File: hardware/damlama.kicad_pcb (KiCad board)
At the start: 2 copper layers, 91 x 90 mm, 63 parts, among them J1 173950578, J2 173950378, J3 SW, J4 PJ-002A, J5 RELAY, J6 SENSOR, J8 629105150521, K1 SRD-05VDC-SL-C, Q1 BC847, SW1 BTN_ACT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

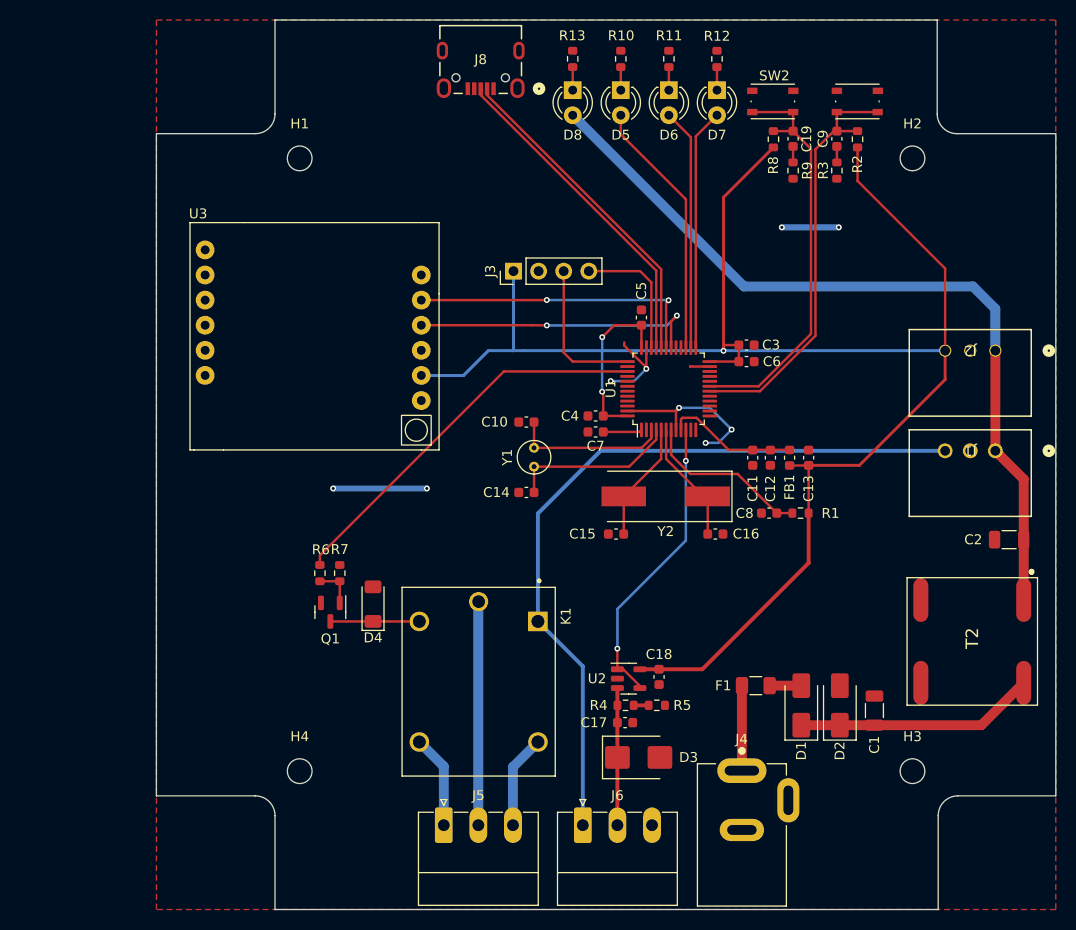
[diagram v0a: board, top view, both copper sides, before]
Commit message: MCU BOOT0 mistake fixed
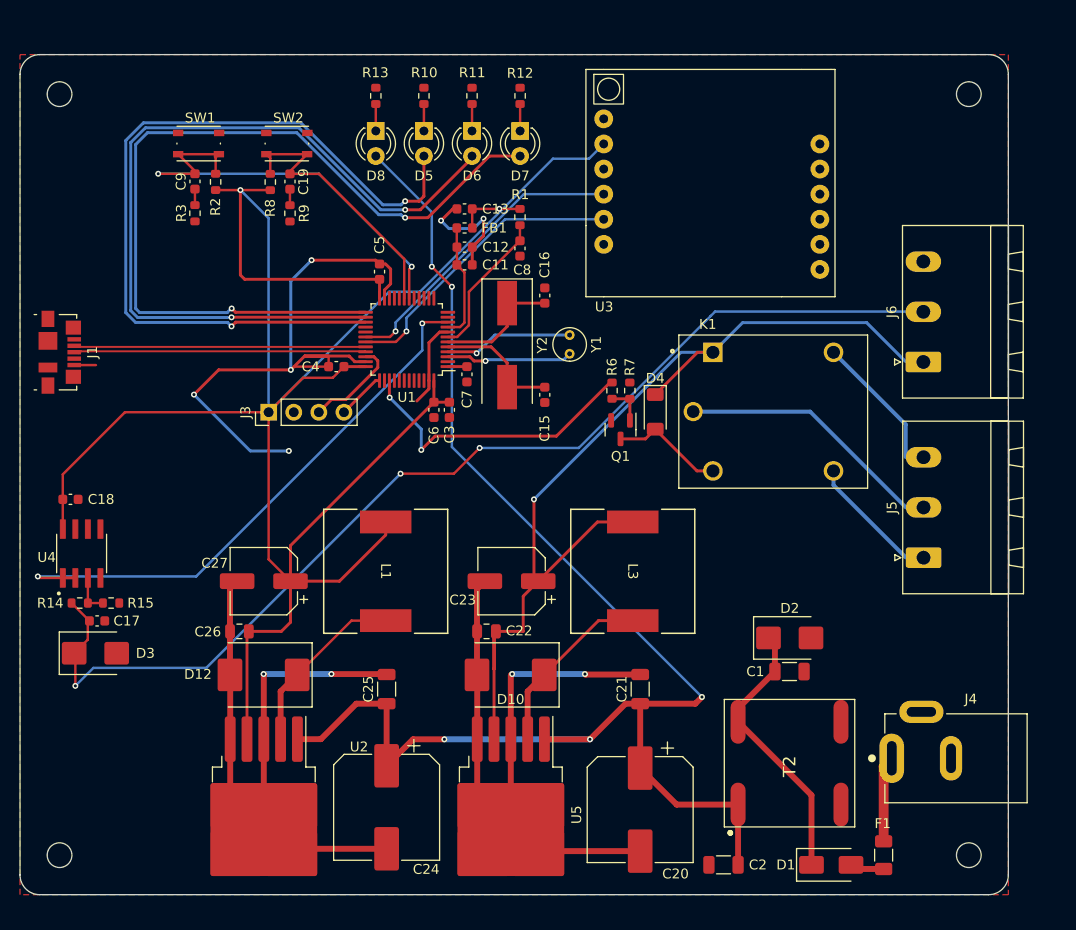
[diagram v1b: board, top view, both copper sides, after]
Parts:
- removed C10, C14: 12.5pF, Capacitor_SMD:C_0603_1608Metric
- removed J2: 173950378, Damlama:Wurth_Power_173950378
- removed J8: 629105150521, Damlama:CONN_USB_WURTH_629105150521
- removed R4: 150, Resistor_SMD:R_0603_1608Metric
- removed R5: 15, Resistor_SMD:R_0603_1608Metric
- added C20: 100uF/63V, Capacitor_SMD:CP_Elec_10x10.5, F.Cu at (142.7, 131.4)
- added C21: 470nF/100V, Capacitor_SMD:C_1206_3216Metric, F.Cu at (142.7, 119.2)
- added C22: 100nF/20V, Capacitor_SMD:C_0805_2012Metric, F.Cu at (127.2, 113.4)
- added C23: 100uF/20V, Capacitor_SMD:CP_Elec_6.3x7.7, F.Cu at (129.7, 108.3)
- added C24: 100uF/63V, Capacitor_SMD:CP_Elec_10x10.5, F.Cu at (117.1, 131.2)
- added C25: 470nF/100V, Capacitor_SMD:C_1206_3216Metric, F.Cu at (117.1, 119.2)
- added C26: 100nF/20V, Capacitor_SMD:C_0805_2012Metric, F.Cu at (102.2, 113.4)
- added C27: 100uF/20V, Capacitor_SMD:CP_Elec_6.3x7.7, F.Cu at (104.7, 108.3)
- added D10: SK56, Diode_SMD:D_SMC, F.Cu at (129.6, 117.8)
- added D12: SK56, Diode_SMD:D_SMC, F.Cu at (104.6, 117.8)
- added L1: 74477020, Damlama:IND_1280-WE-PD_WRE, F.Cu at (117.0, 107.3)
- added L3: 74477020, Damlama:IND_1280-WE-PD_WRE, F.Cu at (142.0, 107.3)
- added R14: 10K, Resistor_SMD:R_0603_1608Metric, F.Cu at (86.0, 110.5)
- added R15: 27K, Resistor_SMD:R_0603_1608Metric, F.Cu at (89.2, 110.5)
- added U4: LM358, Damlama:SOIC127P599X175-8N, F.Cu at (86.2, 105.5)
- added U5: LM2596S-5, Package_TO_SOT_SMD:TO-263-5_TabPin3, F.Cu at (129.7, 131.9)
- D2: footprint Diode_SMD:D_SMA -> Diode_SMD:D_SMB
- F1: value 1A -> 3A
- J1: value 173950578 -> USB_B_Micro; footprint Damlama:Wurth_Power_173950578 -> Connector_USB:USB_Micro-B_Molex_47346-0001
- J5, J6: footprint Connector_Phoenix_MC:PhoenixContact_MC_1,5_3-G-3.5_1x03_P3.50mm_Horizontal -> Connector_Phoenix_MSTB:PhoenixContact_MSTBA_2,5_3-G-5,08_1x03_P5.08mm_Horizontal
- K1: value SRD-05VDC-SL-C -> R6
- U2: value AD8603 -> LM2596S-3.3; footprint Package_TO_SOT_SMD:TSOT-23-5 -> Package_TO_SOT_SMD:TO-263-5_TabPin3
- moved J1 95.2 mm to (84.0, 85.1), turned to -90 degrees
- moved SW1 66.8 mm to (98.1, 64.0)
- moved C9 65.1 mm to (97.7, 67.8)
- moved R2 65.1 mm to (99.8, 67.9)
- moved R3 65.1 mm to (97.7, 71.1)
- moved C18 62.2 mm to (85.1, 100.0), turned to 0 degrees
- moved J6 58.2 mm to (171.4, 86.1), turned to 90 degrees
- moved D3 56.0 mm to (87.6, 115.6)
- moved J5 55.6 mm to (171.4, 105.9), turned to 90 degrees
- moved C17 54.4 mm to (87.8, 112.3)
- moved C19 51.1 mm to (107.3, 67.8)
- moved R9 51.1 mm to (107.3, 71.1)
- moved R8 51.1 mm to (105.3, 67.9)
- moved SW2 49.4 mm to (107.0, 64.0)
- moved C2 43.8 mm to (151.2, 137.0)
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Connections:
- D4 pad 1: Net-(D4-K) -> +5V
- D4 pad 2: GND -> Net-(D4-A)
- J1 pad 1: /Power/+12V -> unconnected-(J1-VBUS-Pad1)
- J1 pad 2: GND -> /MCU/USB_D-
- J1 pad 3: +5V -> /MCU/USB_D+
- J3 pad 3: /MCU/SWCLK -> /MCU/SWDIO
- J3 pad 4: /MCU/SWDIO -> /MCU/SWCLK
- K1 pad A2: Net-(D4-K) -> Net-(D4-A)
- Q1 pad 3: Net-(D4-K) -> Net-(D4-A)
- R6 pad 1: Net-(Q1-B) -> /MCU/RELAY
- R6 pad 2: /MCU/RELAY -> Net-(Q1-B)
- U1 pad 32: /MCU/USB_DM -> /MCU/USB_D-
- U1 pad 33: /MCU/USB_DP -> /MCU/USB_D+
- U2 pad 1: /ADC/ADC -> /Power/+12V
- U2 pad 2: GND -> Net-(D12-K)
- U2 pad 3: /ADC/SENSOR -> Net-(D12-A)
- U2 pad 4: /ADC/ADC -> +3V3
- U2 pad 5: +3V3 -> Net-(D12-A)
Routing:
- net /ADC/SENSOR: track 13.9 -> 109.4 mm, vias 0 -> 3
- net /Power/+12V: track 81.5 -> 148.6 mm, vias 0 -> 5
- net Net-(D12-A): track 0.00 -> 64.7 mm, vias 0 -> 2
- net Net-(D10-A): track 0.00 -> 62.5 mm, vias 0 -> 2
- net /MCU/LED_ERR: track 24.4 -> 85.9 mm, vias 0 -> 2
- net /MCU/LED_DEACT: track 24.4 -> 82.0 mm, vias 0 -> 2
- net /MCU/LED_ACT: track 26.2 -> 81.2 mm, vias 0 -> 2
- net GND: track 44.2 -> 85.5 mm, vias 9 -> 6
- net +3V3: track 186.1 -> 225.4 mm, vias 3 -> 2
- net /MCU/USB_DP: track 33.6 -> 0.00 mm
- net /MCU/USB_DM: track 33.5 -> 0.00 mm
- net /MCU/USB_D+: track 0.00 -> 29.1 mm
- net /MCU/USB_D-: track 0.00 -> 29.0 mm
- net /ADC/ADC: track 30.3 -> 58.9 mm
- net +5V: track 77.3 -> 97.4 mm, vias 0 -> 1
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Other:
- board size 91 x 90 mm -> 100 x 85 mm
- board text added: "DAMLAMA SULAMA KONTROL VE UYARI KARTI"
- board text added: "TASARIM PROJESİ YAREN CAM ELIF ALTIPARMAK"
